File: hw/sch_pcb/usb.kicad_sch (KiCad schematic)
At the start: 13 parts, among them J4 USBC_USB4105-GF-A, U7 USBLC6-2SC6, U9 FT231XQ

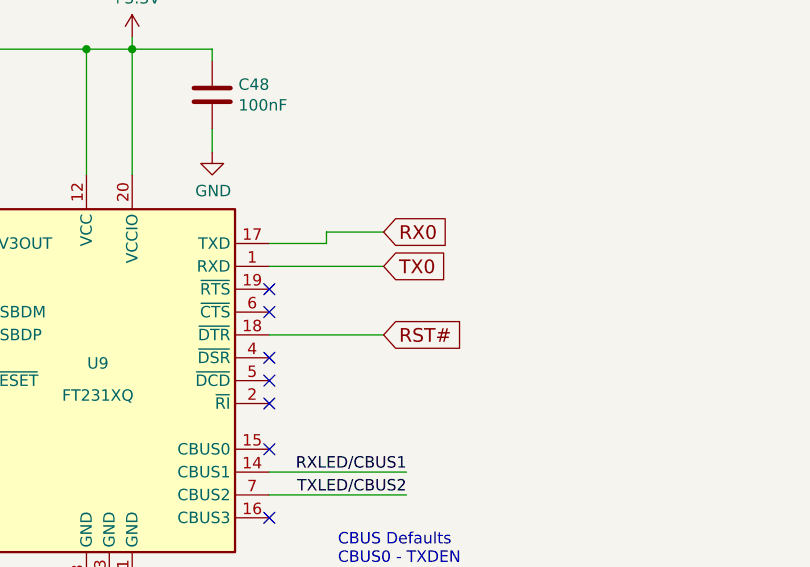
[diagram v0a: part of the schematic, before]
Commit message: Update schematics symbols Add protection  resistor to external connectors. Reorganising digital part of PCB.
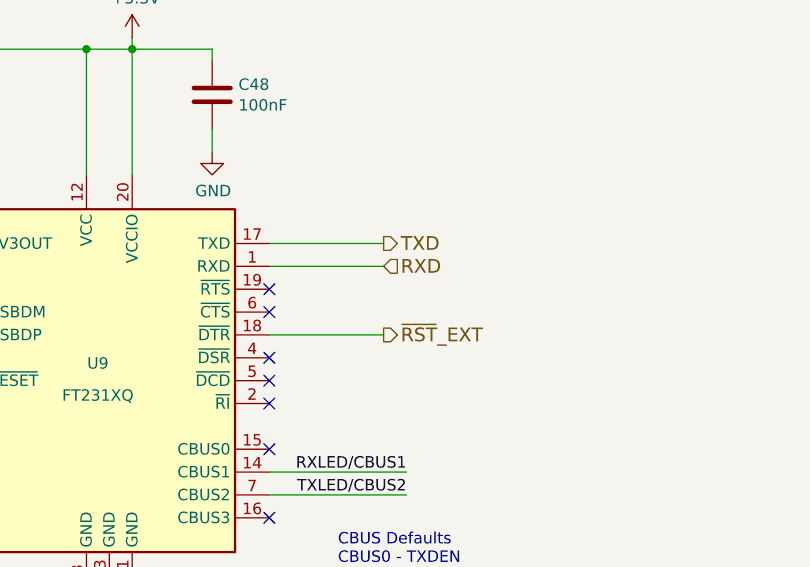
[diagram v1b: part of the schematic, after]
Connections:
- net RST# renamed ~{RST}_EXT
- net RX0 renamed TXD
- net TX0 renamed RXD
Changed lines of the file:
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@@
     (stroke (width 0) (type solid))
   )
-  (wire (pts (xy 166.37 95.25) (xy 172.72 95.25))
+  (wire (pts (xy 166.37 95.25) (xy 179.07 95.25))
     (stroke (width 0) (type default))
   )
@@
     (stroke (width 0) (type solid))
   )
-  (wire (pts (xy 172.72 95.25) (xy 172.72 93.98))
-    (stroke (width 0) (type default))
-  )
   (wire (pts (xy 49.53 127) (xy 49.53 128.27))
     (stroke (width 0) (type solid))
@@
   (wire (pts (xy 67.31 69.85) (xy 67.31 71.12))
     (stroke (width 0) (type solid))
-  )
-  (wire (pts (xy 172.72 93.98) (xy 179.07 93.98))
-    (stroke (width 0) (type default))
   )
   (wire (pts (xy 128.27 102.87) (xy 130.81 102.87))
@@
     (effects (font (size 1.27 1.27)) (justify right bottom))
   )
-  (global_label "RST#" (shape input) (at 179.07 105.41 0) (fields_autoplaced)
+  (hierarchical_label "TXD" (shape output) (at 179.07 95.25 0) (fields_autoplaced)
     (effects (font (size 1.524 1.524)) (justify left))
-    (property "Intersheetrefs" "${INTERSHEET_REFS}" (at 187.8548 105.5052 0)
-      (effects (font (size 1.524 1.524)) (justify left) hide)
-    )
-  )
-  (global_label "TX0" (shape input) (at 179.07 97.79 0) (fields_autoplaced)
-    (effects (font (size 1.524 1.524)) (justify left))
-    (property "Intersheetrefs" "${INTERSHEET_REFS}" (at 186.2582 97.6948 0)
-      (effects (font (size 1.524 1.524)) (justify left) hide)
-    )
-  )
-  (global_label "RX0" (shape input) (at 179.07 93.98 0) (fields_autoplaced)
-    (effects (font (size 1.524 1.524)) (justify left))
-    (property "Intersheetrefs" "${INTERSHEET_REFS}" (at 186.6211 93.8848 0)
-      (effects (font (size 1.524 1.524)) (justify left) hide)
-    )
   )
   (hierarchical_label "VUSB" (shape input) (at 64.77 48.26 90) (fields_autoplaced)
     (effects (font (size 1.524 1.524)) (justify left))
   )
+  (hierarchical_label "~{RST}_EXT" (shape output) (at 179.07 105.41 0) (fields_autoplaced)
+    (effects (font (size 1.524 1.524)) (justify left))
+  )
+  (hierarchical_label "RXD" (shape input) (at 179.07 97.79 0) (fields_autoplaced)
+    (effects (font (size 1.524 1.524)) (justify left))
+  )

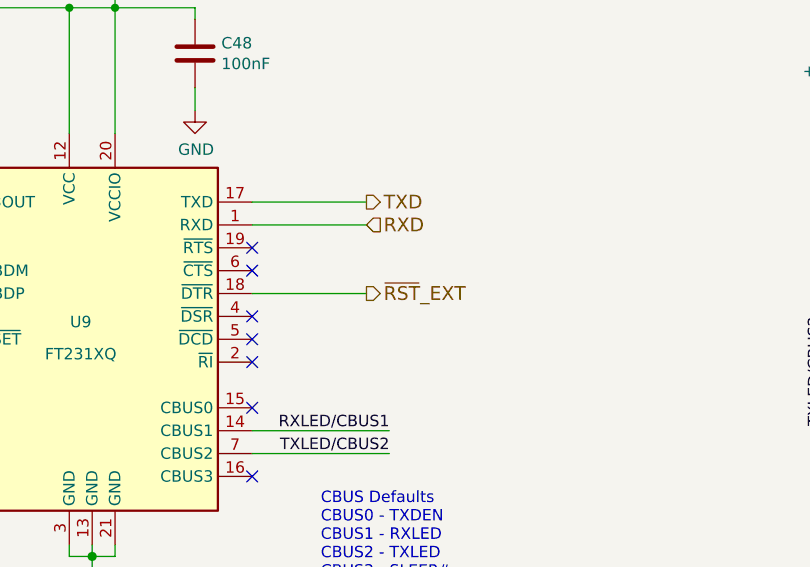
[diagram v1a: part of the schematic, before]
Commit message: Angled USB IC.
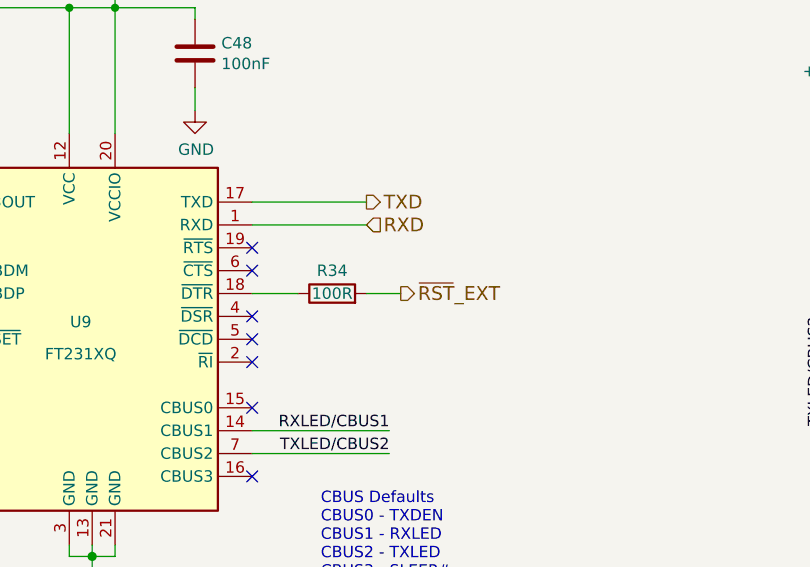
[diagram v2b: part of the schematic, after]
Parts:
- added R34: 100R, Resistor_SMD:R_0805_2012Metric, symbol Device:R
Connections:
- net ~{RST}_EXT: now also R34.2; no longer U9.18 (~{DTR})
- new net: R34.1, U9.18 (~{DTR})
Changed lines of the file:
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@@
     (stroke (width 0) (type solid))
+  )
+  (wire (pts (xy 179.07 105.41) (xy 182.88 105.41))
+    (stroke (width 0) (type default))
   )
   (wire (pts (xy 64.77 52.07) (xy 71.12 52.07))
     (stroke (width 0) (type default))
   )
-  (wire (pts (xy 166.37 105.41) (xy 179.07 105.41))
-    (stroke (width 0) (type default))
-  )
   (wire (pts (xy 166.37 120.65) (xy 181.61 120.65))
     (stroke (width 0) (type solid))
@@
   (wire (pts (xy 49.53 105.41) (xy 49.53 106.68))
     (stroke (width 0) (type solid))
+  )
+  (wire (pts (xy 166.37 105.41) (xy 171.45 105.41))
+    (stroke (width 0) (type default))
   )
   (wire (pts (xy 128.27 105.41) (xy 130.81 105.41))
@@
     (effects (font (size 1.524 1.524)) (justify left))
   )
-  (hierarchical_label "~{RST}_EXT" (shape output) (at 179.07 105.41 0) (fields_autoplaced)
+  (hierarchical_label "~{RST}_EXT" (shape output) (at 182.88 105.41 0) (fields_autoplaced)
     (effects (font (size 1.524 1.524)) (justify left))
   )
@@
         )
       )
+    )
+  )
+  (symbol (lib_id "Device:R") (at 175.26 105.41 90) (unit 1)
+    (in_bom yes) (on_board yes) (dnp no)
+    (property "Reference" "R34" (at 175.26 102.87 90)
+      (effects (font (size 1.27 1.27)))
+    )
+    (property "Value" "100R" (at 175.26 105.41 90)
+      (effects (font (size 1.27 1.27)))
+    )
+    (property "Footprint" "Resistor_SMD:R_0805_2012Metric" (at 175.26 107.188 90)
+      (effects (font (size 1.27 1.27)) hide)
+    )
+    (property "Datasheet" "~" (at 175.26 105.41 0)
+      (effects (font (size 1.27 1.27)) hide)
+    )
+    (property "UST_ID" "5c70984512875079b91f8977" (at 175.26 105.41 0)
+      (effects (font (size 1.27 1.27)) hide)
+    )
+    (pin "1")
+    (pin "2")
+    (instances
+      (project "USTSIPIN02"
+        (path "/0a87ced0-2af2-43c5-a56c-218f7013d76f/00000000-0000-0000-0000-00005c4aedd8"
+          (reference "R34") (unit 1)
+        )
+        (path "/0a87ced0-2af2-43c5-a56c-218f7013d76f/19d1d659-a959-4bd5-b510-08a4dbcee178"
+          (reference "R48") (unit 1)
+        )
+      )

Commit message: Resolve inconsistent component types.
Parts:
- C45, C48: UST_ID 5c70984812875079b91f8bf2 -> 5c70984712875079b91f8b4c
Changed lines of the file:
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@@
       (effects (font (size 1.27 1.27)) hide)
     )
-    (property "UST_ID" "5c70984812875079b91f8bf2" (at 160.02 78.74 0)
+    (property "UST_ID" "5c70984712875079b91f8b4c" (at 160.02 78.74 0)
       (effects (font (size 1.27 1.27)) hide)
     )
@@
       (effects (font (size 1.27 1.27)) hide)
     )
-    (property "UST_ID" "5c70984812875079b91f8bf2" (at 114.3 99.06 0)
-      (effects (font (size 1.27 1.27)) hide)
-    )
+    (property "UST_ID" "5c70984712875079b91f8b4c" (at 114.3 99.06 0)
+      (effects (font (size 1.27 1.27)) hide)
+    )

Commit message: Fix USTids.
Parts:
- R26: UST_ID 5c70984512875079b91f8960 -> 5c70984612875079b91f8995
- R28, R29: UST_ID 5c70984512875079b91f8957 -> 5c70984512875079b91f897c
- R30, R31: UST_ID 628d1404dc56076e9a223650 -> 5fa0fc3e12875025b3977997
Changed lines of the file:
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@@
       (effects (font (size 1.27 1.27)) hide)
     )
-    (property "UST_ID" "5c70984512875079b91f8957" (at 242.57 101.6 0)
+    (property "UST_ID" "5c70984512875079b91f897c" (at 242.57 101.6 0)
       (effects (font (size 1.27 1.27)) hide)
     )
@@
       (effects (font (size 1.27 1.27)) hide)
     )
-    (property "UST_ID" "5c70984512875079b91f8957" (at 229.87 101.6 0)
+    (property "UST_ID" "5c70984512875079b91f897c" (at 229.87 101.6 0)
       (effects (font (size 1.27 1.27)) hide)
     )
@@
   (symbol (lib_id "Device:R") (at 63.5 59.69 90) (unit 1)
     (in_bom yes) (on_board yes) (dnp no)
-    (property "Reference" "R31" (at 58.42 60.8138 90)
-      (effects (font (size 1.27 1.27)))
-    )
-    (property "Value" "5k1" (at 68.58 61.842 90)
+    (property "Reference" "R31" (at 63.5 62.23 90)
+      (effects (font (size 1.27 1.27)))
+    )
+    (property "Value" "5k1" (at 63.5 59.69 90)
       (effects (font (size 1.27 1.27)))
     )
@@
       (effects (font (size 1.27 1.27)) hide)
     )
-    (property "UST_ID" "628d1404dc56076e9a223650" (at 63.5 59.69 0)
+    (property "UST_ID" "5fa0fc3e12875025b3977997" (at 63.5 59.69 0)
       (effects (font (size 1.27 1.27)) hide)
     )
@@
   (symbol (lib_id "Device:R") (at 63.5 57.15 90) (unit 1)
     (in_bom yes) (on_board yes) (dnp no)
-    (property "Reference" "R30" (at 60.96 54.4638 90)
-      (effects (font (size 1.27 1.27)))
-    )
-    (property "Value" "5k1" (at 68.58 55.492 90)
+    (property "Reference" "R30" (at 63.5 54.61 90)
+      (effects (font (size 1.27 1.27)))
+    )
+    (property "Value" "5k1" (at 63.5 57.15 90)
       (effects (font (size 1.27 1.27)))
     )
@@
       (effects (font (size 1.27 1.27)) hide)
     )
-    (property "UST_ID" "628d1404dc56076e9a223650" (at 63.5 57.15 0)
+    (property "UST_ID" "5fa0fc3e12875025b3977997" (at 63.5 57.15 0)
       (effects (font (size 1.27 1.27)) hide)
     )
@@
       (effects (font (size 1.27 1.27)) hide)
     )
-    (property "UST_ID" "5c70984512875079b91f8960" (at 102.87 104.14 0)
-      (effects (font (size 1.27 1.27)) hide)
-    )
+    (property "UST_ID" "5c70984612875079b91f8995" (at 102.87 104.14 0)
+      (effects (font (size 1.27 1.27)) hide)
+    )

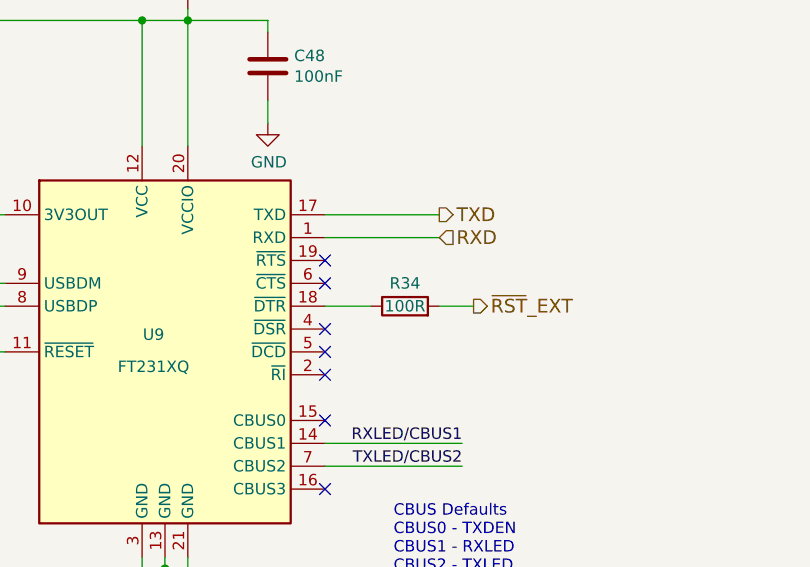
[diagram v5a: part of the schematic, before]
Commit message: Update project to KiCADv8.
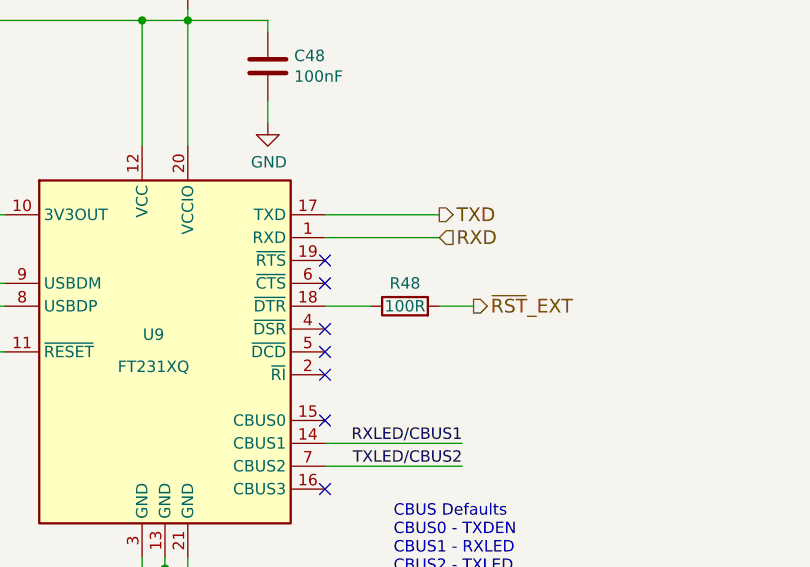
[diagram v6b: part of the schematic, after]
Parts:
- renumbered R34 to R48
